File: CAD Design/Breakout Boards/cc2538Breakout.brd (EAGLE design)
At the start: 70.1 x 35.7 mm, 29 parts

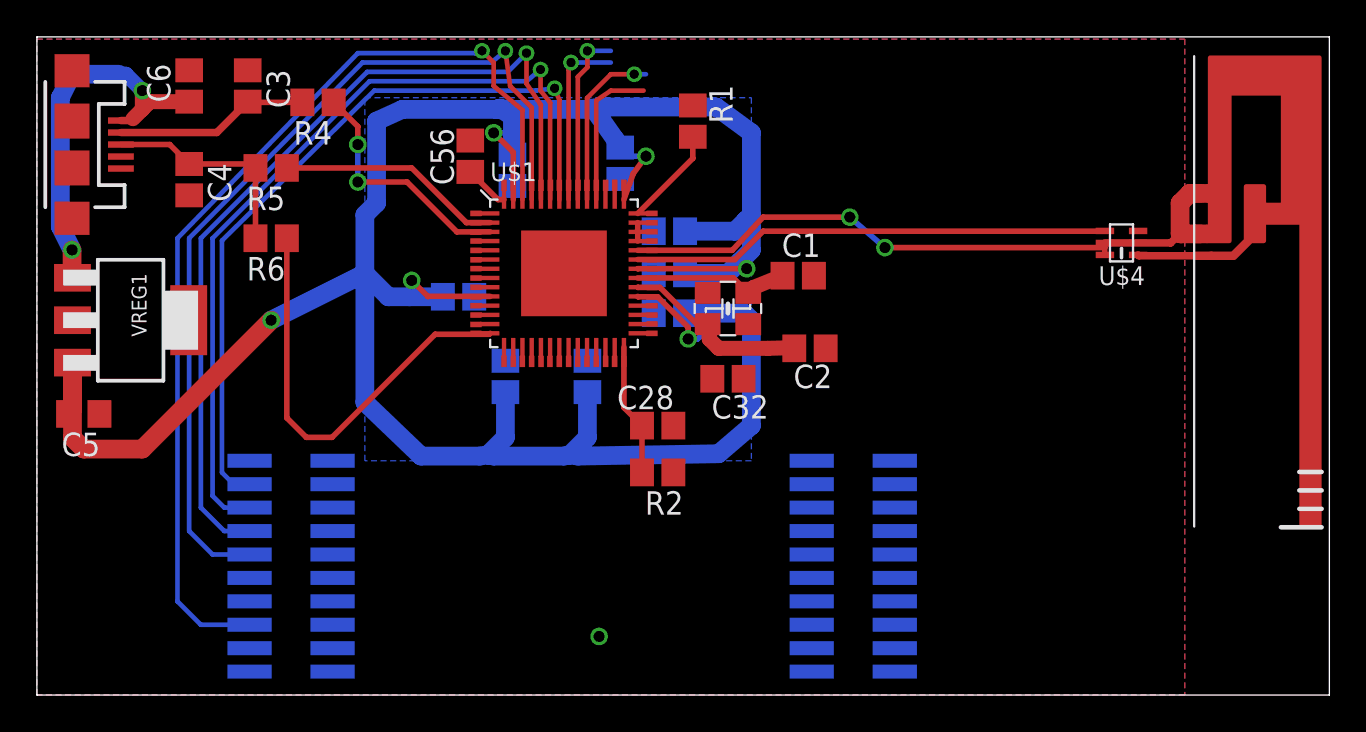
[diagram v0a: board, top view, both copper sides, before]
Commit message: Routing, First DRC complete
cc2538 Breakout ready for design review and final ERC/DRC checks.
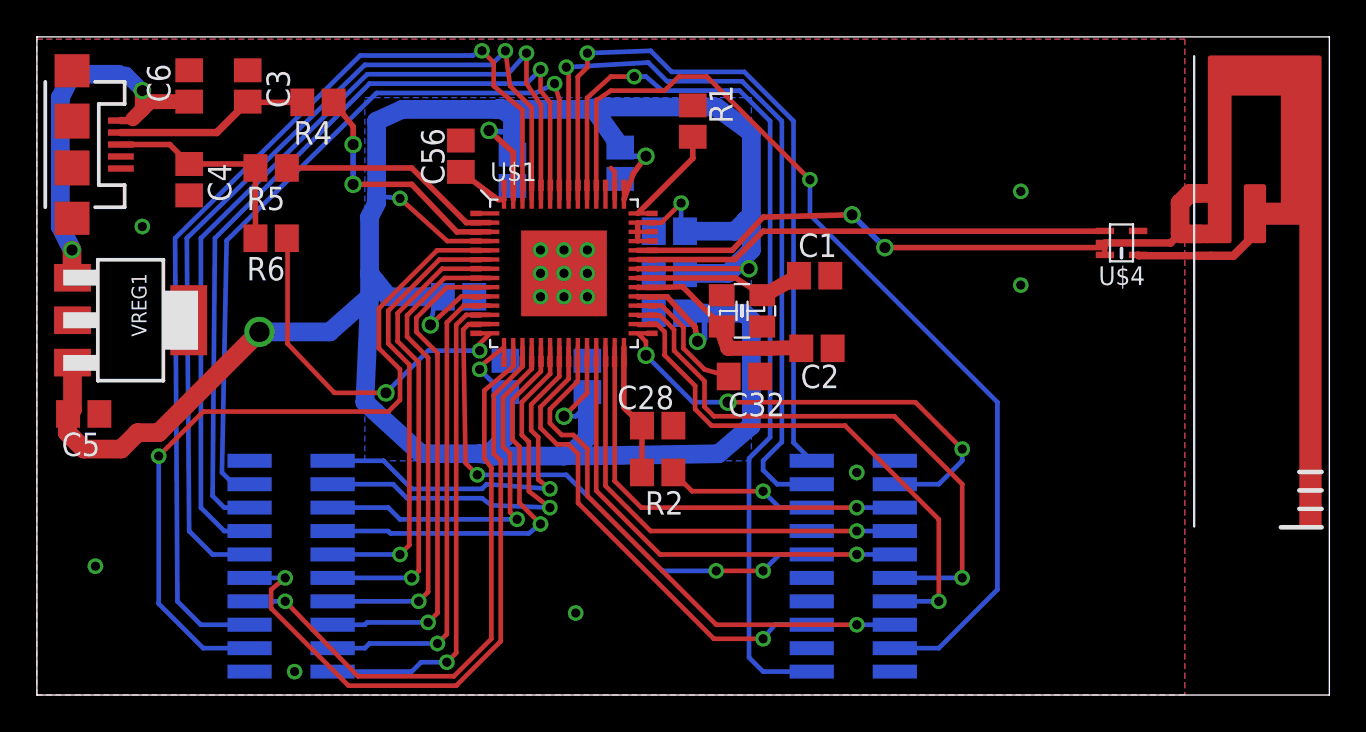
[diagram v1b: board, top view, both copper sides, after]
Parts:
- moved C32 0.90 mm to (38.4, 17.3)
- moved C1 0.89 mm to (42.2, 22.7)
- moved XTAL-32MHZ 0.77 mm to (38.2, 20.8)
- moved C56 0.51 mm to (23.0, 29.2)
- moved C2 0.38 mm to (42.3, 18.8)
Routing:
- net I/O24: track 8.10 -> 53.1 mm, vias 0 -> 1
- net I/O3: track 0.00 -> 41.0 mm, vias 0 -> 1
- net I/O21: track 9.23 -> 50.1 mm
- net I/O9: track 0.00 -> 35.9 mm, vias 0 -> 1
- net I/O37: track 9.61 -> 42.5 mm
- net I/O7: track 0.00 -> 32.3 mm, vias 0 -> 1
- net I/O30: track 0.00 -> 31.6 mm, vias 0 -> 1
- net I/O31: track 0.00 -> 30.4 mm, vias 0 -> 3
- net I/O39: track 9.55 -> 39.7 mm
- net I/O26: track 0.00 -> 29.5 mm, vias 0 -> 1
- net I/O28: track 0.00 -> 29.0 mm, vias 0 -> 1
- net I/O6: track 0.00 -> 27.1 mm, vias 0 -> 1
- net I/O2: track 0.00 -> 27.0 mm, vias 0 -> 1
- net I/O25: track 0.00 -> 26.4 mm, vias 0 -> 1
- net I/O8: track 0.00 -> 26.2 mm, vias 0 -> 1
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
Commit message: cc2538 Breakout_rev1.0
cc2538 Breakout board ready to go to print. Fixed crossed signals on
PC0/PC1, verified headers, second and third DRC’s passed.
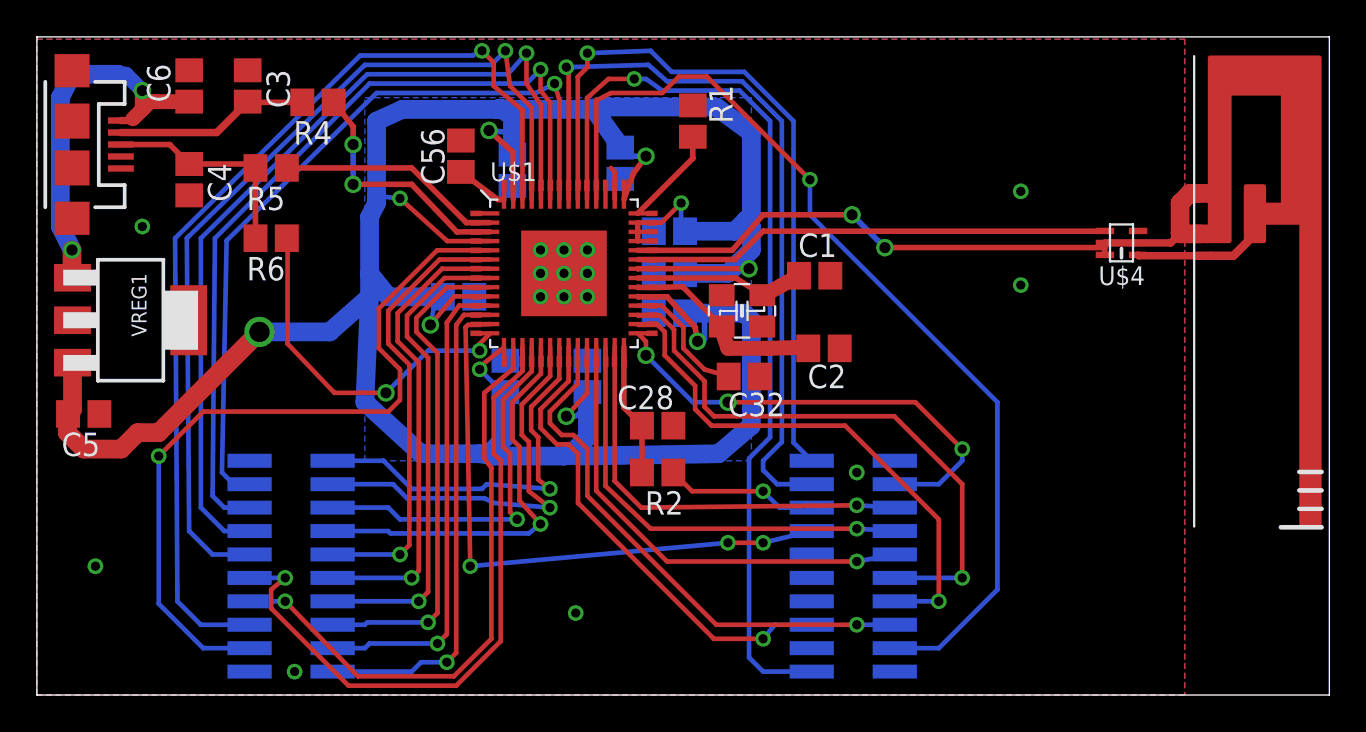
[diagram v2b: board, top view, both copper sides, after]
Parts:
- R6: value 56k -> 1.5k
- moved C2 0.38 mm to (42.7, 18.8)
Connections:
- net I/O31: no longer U$1.13
- net I/O33: now also U$1.13
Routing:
- net I/O33: track 0.00 -> 33.0 mm, vias 0 -> 3
- net I/O31: track 30.4 -> 0.00 mm, vias 3 -> 0
